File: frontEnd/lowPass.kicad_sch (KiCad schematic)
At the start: 19 parts, among them U201 BGS12P2L6E6327XTSA1, U202 BGS12P2L6E6327XTSA1

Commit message: assign footprints, part designators
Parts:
- U201, U202: footprint (none) -> frontEnd:BGS12P2L6E6327XTSA1
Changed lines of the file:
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@@
   (symbol (lib_id "power:+3V3") (at 41.91 163.83 0) (unit 1)
     (in_bom yes) (on_board yes)
-    (property "Reference" "#PWR?" (id 0) (at 41.91 167.64 0)
+    (property "Reference" "#PWR0145" (id 0) (at 41.91 167.64 0)
       (effects (font (size 1.27 1.27)) hide)
     )
@@
   (symbol (lib_id "power:GND") (at 41.91 173.99 0) (unit 1)
     (in_bom yes) (on_board yes)
-    (property "Reference" "#PWR?" (id 0) (at 41.91 180.34 0)
+    (property "Reference" "#PWR0146" (id 0) (at 41.91 180.34 0)
       (effects (font (size 1.27 1.27)) hide)
     )
@@
   (symbol (lib_id "power:GND") (at 127 83.82 0) (unit 1)
     (in_bom yes) (on_board yes)
-    (property "Reference" "#PWR?" (id 0) (at 127 90.17 0)
+    (property "Reference" "#PWR0138" (id 0) (at 127 90.17 0)
       (effects (font (size 1.27 1.27)) hide)
     )
@@
   (symbol (lib_id "power:GND") (at 104.14 83.82 0) (unit 1)
     (in_bom yes) (on_board yes)
-    (property "Reference" "#PWR?" (id 0) (at 104.14 90.17 0)
+    (property "Reference" "#PWR0131" (id 0) (at 104.14 90.17 0)
       (effects (font (size 1.27 1.27)) hide)
     )
@@
   (symbol (lib_id "power:GND") (at 92.71 83.82 0) (unit 1)
     (in_bom yes) (on_board yes)
-    (property "Reference" "#PWR?" (id 0) (at 92.71 90.17 0)
+    (property "Reference" "#PWR0130" (id 0) (at 92.71 90.17 0)
       (effects (font (size 1.27 1.27)) hide)
     )
@@
   (symbol (lib_id "power:GND") (at 50.8 119.38 0) (unit 1)
     (in_bom yes) (on_board yes)
-    (property "Reference" "#PWR?" (id 0) (at 50.8 125.73 0)
+    (property "Reference" "#PWR0147" (id 0) (at 50.8 125.73 0)
       (effects (font (size 1.27 1.27)) hide)
     )
@@
   (symbol (lib_id "power:GND") (at 207.01 83.82 0) (unit 1)
     (in_bom yes) (on_board yes)
-    (property "Reference" "#PWR?" (id 0) (at 207.01 90.17 0)
+    (property "Reference" "#PWR0140" (id 0) (at 207.01 90.17 0)
       (effects (font (size 1.27 1.27)) hide)
     )
@@
   (symbol (lib_id "power:GND") (at 161.29 83.82 0) (unit 1)
     (in_bom yes) (on_board yes)
-    (property "Reference" "#PWR?" (id 0) (at 161.29 90.17 0)
+    (property "Reference" "#PWR0135" (id 0) (at 161.29 90.17 0)
       (effects (font (size 1.27 1.27)) hide)
     )
@@
   (symbol (lib_id "power:GND") (at 184.15 83.82 0) (unit 1)
     (in_bom yes) (on_board yes)
-    (property "Reference" "#PWR?" (id 0) (at 184.15 90.17 0)
+    (property "Reference" "#PWR0143" (id 0) (at 184.15 90.17 0)
       (effects (font (size 1.27 1.27)) hide)
     )
@@
       (effects (font (size 1.27 1.27)) (justify right))
     )
-    (property "Footprint" "" (id 2) (at 243.84 78.74 0)
+    (property "Footprint" "frontEnd:BGS12P2L6E6327XTSA1" (id 2) (at 243.84 78.74 0)
       (effects (font (size 1.27 1.27)) hide)
     )
@@
   (symbol (lib_id "power:GND") (at 195.58 83.82 0) (unit 1)
     (in_bom yes) (on_board yes)
-    (property "Reference" "#PWR?" (id 0) (at 195.58 90.17 0)
+    (property "Reference" "#PWR0144" (id 0) (at 195.58 90.17 0)
       (effects (font (size 1.27 1.27)) hide)
     )
@@
   (symbol (lib_id "power:+3V3") (at 60.96 69.85 0) (unit 1)
     (in_bom yes) (on_board yes)
-    (property "Reference" "#PWR?" (id 0) (at 60.96 73.66 0)
+    (property "Reference" "#PWR0132" (id 0) (at 60.96 73.66 0)
       (effects (font (size 1.27 1.27)) hide)
     )
@@
       (effects (font (size 1.27 1.27)) (justify right))
     )
-    (property "Footprint" "" (id 2) (at 54.61 78.74 0)
+    (property "Footprint" "frontEnd:BGS12P2L6E6327XTSA1" (id 2) (at 54.61 78.74 0)
       (effects (font (size 1.27 1.27)) hide)
     )
@@
   (symbol (lib_id "power:GND") (at 172.72 83.82 0) (unit 1)
     (in_bom yes) (on_board yes)
-    (property "Reference" "#PWR?" (id 0) (at 172.72 90.17 0)
+    (property "Reference" "#PWR0134" (id 0) (at 172.72 90.17 0)
       (effects (font (size 1.27 1.27)) hide)
     )
@@
   (symbol (lib_id "power:GND") (at 138.43 83.82 0) (unit 1)
     (in_bom yes) (on_board yes)
-    (property "Reference" "#PWR?" (id 0) (at 138.43 90.17 0)
+    (property "Reference" "#PWR0137" (id 0) (at 138.43 90.17 0)
       (effects (font (size 1.27 1.27)) hide)
     )
@@
   (symbol (lib_id "power:GND") (at 149.86 83.82 0) (unit 1)
     (in_bom yes) (on_board yes)
-    (property "Reference" "#PWR?" (id 0) (at 149.86 90.17 0)
+    (property "Reference" "#PWR0136" (id 0) (at 149.86 90.17 0)
       (effects (font (size 1.27 1.27)) hide)
     )
@@
   (symbol (lib_id "power:GND") (at 60.96 91.44 0) (unit 1)
     (in_bom yes) (on_board yes)
-    (property "Reference" "#PWR?" (id 0) (at 60.96 97.79 0)
+    (property "Reference" "#PWR0133" (id 0) (at 60.96 97.79 0)
       (effects (font (size 1.27 1.27)) hide)
     )
@@
   (symbol (lib_id "power:+3V3") (at 237.49 69.85 0) (unit 1)
     (in_bom yes) (on_board yes)
-    (property "Reference" "#PWR?" (id 0) (at 237.49 73.66 0)
+    (property "Reference" "#PWR0141" (id 0) (at 237.49 73.66 0)
       (effects (font (size 1.27 1.27)) hide)
     )
@@
   (symbol (lib_id "power:GND") (at 237.49 91.44 0) (unit 1)
     (in_bom yes) (on_board yes)
-    (property "Reference" "#PWR?" (id 0) (at 237.49 97.79 0)
+    (property "Reference" "#PWR0142" (id 0) (at 237.49 97.79 0)
       (effects (font (size 1.27 1.27)) hide)
     )
@@
   (symbol (lib_id "power:GND") (at 115.57 83.82 0) (unit 1)
     (in_bom yes) (on_board yes)
-    (property "Reference" "#PWR?" (id 0) (at 115.57 90.17 0)
-      (effects (font (size 1.27 1.27)) hide)
-    )
+    (property "Reference" "#PWR0139" (id 0) (at 115.57 90.17 0)
+      (effects (font (size 1.27 1.27)) hide)
+    )

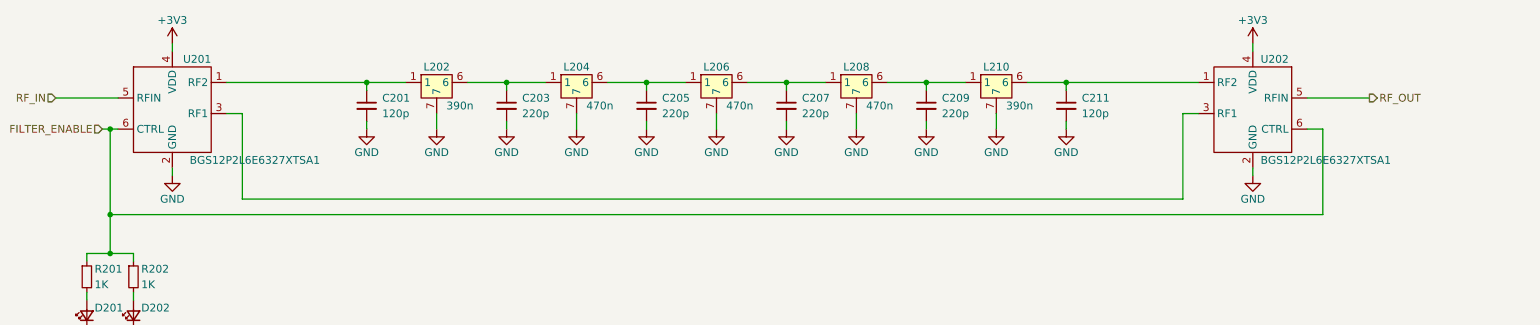
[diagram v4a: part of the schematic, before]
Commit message: convert all embeded filter to plug-in modules, start pcb layout
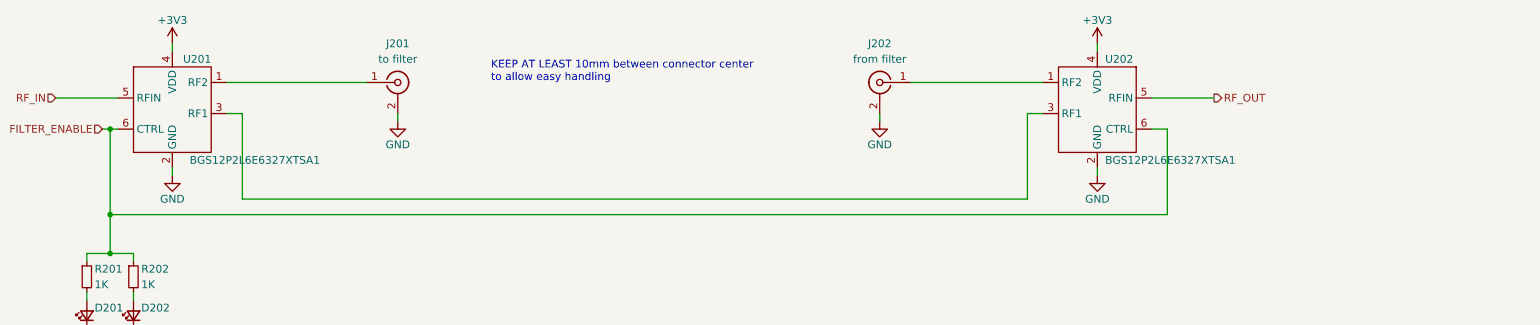
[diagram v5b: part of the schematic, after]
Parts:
- removed C201, C211: 120p, Capacitor_SMD:C_0805_2012Metric, symbol Device:C_Small
- removed C203, C205, C207, C209: 220p, Capacitor_SMD:C_0805_2012Metric, symbol Device:C_Small
- removed L202, L210: 390n, frontEnd:TOKO_10K, symbol frontEnd:TOKO_10K_SERIES
- removed L204, L206, L208: 470n, frontEnd:TOKO_10K, symbol frontEnd:TOKO_10K_SERIES
- added J201: to filter, frontEnd:SMA_FEM_TH_VERTICAL, symbol Connector:Conn_Coaxial
- added J202: from filter, frontEnd:SMA_FEM_TH_VERTICAL, symbol Connector:Conn_Coaxial
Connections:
- net GND: now also J201.2 (Ext), J202.2 (Ext)
- net at U201.1 (RF2): now also J201.1 (In)
- net at U202.1 (RF2): now also J202.1 (In)
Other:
- note added: "KEEP AT LEAST 10mm between connector center to allow easy handling"
- moved on the sheet: U202
